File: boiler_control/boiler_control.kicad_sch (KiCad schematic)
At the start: 37 parts, among them J1 Conn_01x01, J3V3 Conn_01x03, J5V1 Conn_01x03, U2 MOUDLE-SEEEDUINO-XIAO-ESP32C3

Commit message: Replace max3856 with SSOP package; replace all 0201 res/cap packages with 0603
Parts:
- removed C1, C2, C4, C5: 100n, Capacitor_SMD:C_0201_0603Metric_Pad0.64x0.40mm_HandSolder, symbol Device:C
- removed C3, C6: 100nF, Capacitor_SMD:C_0201_0603Metric_Pad0.64x0.40mm_HandSolder, symbol Device:C
- removed JPTa1, JPTb1: Conn_01x02, Connector_PinHeader_2.54mm:PinHeader_1x02_P2.54mm_Vertical, symbol Connector_Generic:Conn_01x02
- removed R1, R2, R3, R7: 1k, Resistor_SMD:R_0201_0603Metric_Pad0.64x0.40mm_HandSolder, symbol Device:R
- removed Rref1, Rref2: R, Resistor_SMD:R_0201_0603Metric_Pad0.64x0.40mm_HandSolder, symbol Device:R
- removed UPTA1, UPTB1: MAX31865xTP, Package_DFN_QFN:TQFN-20-1EP_5x5mm_P0.65mm_EP3.25x3.25mm, symbol Sensor_Temperature:MAX31865xTP
- R4, R5, R6: footprint Resistor_SMD:R_0201_0603Metric_Pad0.64x0.40mm_HandSolder -> Resistor_SMD:R_0603_1608Metric_Pad0.98x0.95mm_HandSolder
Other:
- added sheet bottom_max (bottom_max.kicad_sch)
- note removed: "0.1%"
- note removed: "430 Ohm for PT100 4.3 kOhm for PT1000"

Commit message: Updating to v1.4 - pushed to order
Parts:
- J1: footprint Connector_PinHeader_1.00mm:PinHeader_1x01_P1.00mm_Vertical -> Connector_PinHeader_2.54mm:PinHeader_1x01_P2.54mm_Vertical
- R21: value R -> 100
- R22: value R -> 330
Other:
- moved on the sheet: D4, D5, H1, H2, H3, H4, J1, J3V3, J5V1, JDisplay1, JGND1, JGND2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

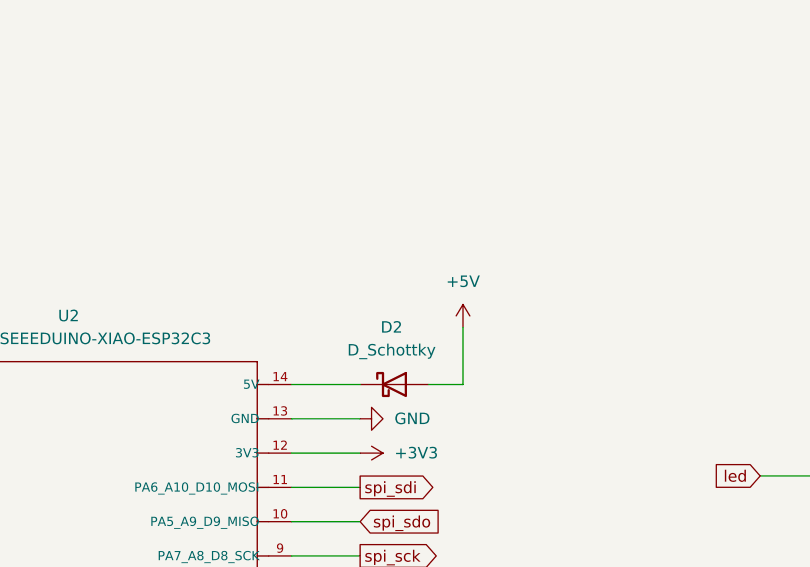
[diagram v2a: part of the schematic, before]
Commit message: Adding JB1 jumper for bridge change size of connectors for pt1000 to 3.5 mm some cosmetics
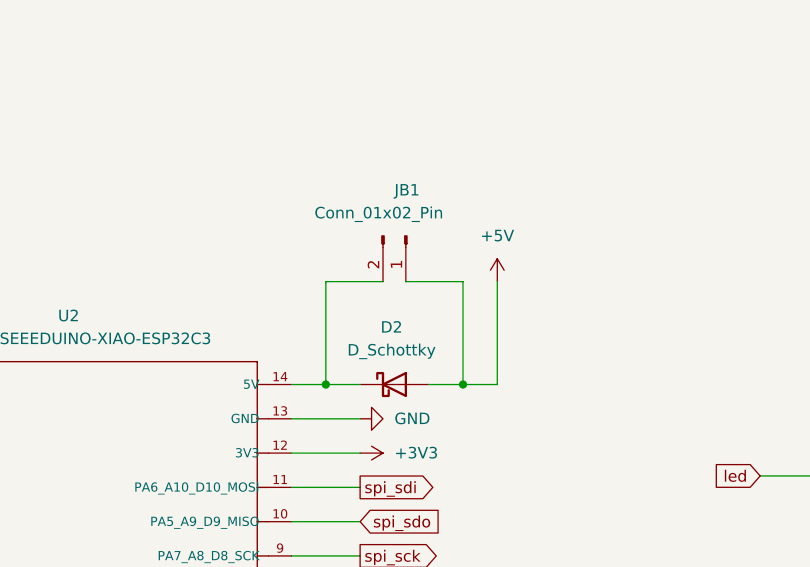
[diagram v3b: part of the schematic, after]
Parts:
- added JB1: Conn_01x02_Pin, Connector_PinHeader_2.54mm:PinHeader_1x02_P2.54mm_Vertical, symbol Connector:Conn_01x02_Pin
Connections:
- net +5V: now also JB1.1 (Pin_1)
- net at D2.1 (K), U2.14 (5V): now also JB1.2 (Pin_2)
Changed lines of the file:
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@@
   (junction (at 139.7 133.35) (diameter 0) (color 0 0 0 0)
   )
+  (junction (at 114.3 38.1) (diameter 0) (color 0 0 0 0)
+  )
   (junction (at 59.69 123.19) (diameter 0) (color 0 0 0 0)
   )
@@
   (junction (at 69.85 125.73) (diameter 0) (color 0 0 0 0)
   )
+  (junction (at 99.06 38.1) (diameter 0) (color 0 0 0 0)
+  )
   (junction (at 208.28 72.39) (diameter 0) (color 0 0 0 0)
   )
@@
     (stroke (width 0) (type default))
   )
+  (wire (pts (xy 99.06 26.67) (xy 99.06 38.1))
+    (stroke (width 0) (type default))
+  )
   (wire (pts (xy 95.25 57.15) (xy 102.87 57.15))
     (stroke (width 0) (type default))
@@
     (stroke (width 0) (type default))
   )
+  (wire (pts (xy 105.41 26.67) (xy 99.06 26.67))
+    (stroke (width 0) (type default))
+  )
   (wire (pts (xy 95.25 45.72) (xy 102.87 45.72))
     (stroke (width 0) (type default))
@@
     (stroke (width 0) (type default))
   )
+  (wire (pts (xy 118.11 26.67) (xy 118.11 38.1))
+    (stroke (width 0) (type default))
+  )
   (wire (pts (xy 95.25 53.34) (xy 102.87 53.34))
     (stroke (width 0) (type default))
@@
     (stroke (width 0) (type default))
   )
+  (wire (pts (xy 114.3 26.67) (xy 114.3 38.1))
+    (stroke (width 0) (type default))
+  )
   (wire (pts (xy 69.85 125.73) (xy 69.85 128.27))
     (stroke (width 0) (type default))
@@
     (stroke (width 0) (type default))
   )
-  (wire (pts (xy 114.3 38.1) (xy 114.3 31.75))
-    (stroke (width 0) (type default))
-  )
   (wire (pts (xy 59.69 116.84) (xy 59.69 123.19))
     (stroke (width 0) (type default))
@@
     (stroke (width 0) (type default))
   )
+  (wire (pts (xy 107.95 26.67) (xy 114.3 26.67))
+    (stroke (width 0) (type default))
+  )
   (wire (pts (xy 69.85 123.19) (xy 69.85 125.73))
     (stroke (width 0) (type default))
@@
     (stroke (width 0) (type default))
   )
+  (wire (pts (xy 114.3 38.1) (xy 118.11 38.1))
+    (stroke (width 0) (type default))
+  )
   (wire (pts (xy 66.04 139.7) (xy 69.85 139.7))
     (stroke (width 0) (type default))
   )
+  (wire (pts (xy 99.06 38.1) (xy 102.87 38.1))
+    (stroke (width 0) (type default))
+  )
   (wire (pts (xy 38.1 60.96) (xy 45.72 60.96))
     (stroke (width 0) (type default))
@@
     (stroke (width 0) (type default))
   )
-  (wire (pts (xy 95.25 38.1) (xy 102.87 38.1))
+  (wire (pts (xy 95.25 38.1) (xy 99.06 38.1))
     (stroke (width 0) (type default))
   )
@@
     )
   )
+  (symbol (lib_id "Connector:Conn_01x02_Pin") (at 107.95 21.59 270) (unit 1)
+    (in_bom yes) (on_board yes) (dnp no)
+    (property "Reference" "JB1" (at 106.68 16.51 90)
+      (effects (font (size 1.27 1.27)) (justify left))
+    )
+    (property "Value" "Conn_01x02_Pin" (at 97.79 19.05 90)
+      (effects (font (size 1.27 1.27)) (justify left))
+    )
+    (property "Footprint" "Connector_PinHeader_2.54mm:PinHeader_1x02_P2.54mm_Vertical" (at 107.95 21.59 0)
+      (effects (font (size 1.27 1.27)) hide)
+    )
+    (property "Datasheet" "~" (at 107.95 21.59 0)
+      (effects (font (size 1.27 1.27)) hide)
+    )
+    (pin "1")
+    (pin "2")
+    (instances
+      (project "boiler_control"
+        (path "/42805374-cffb-434a-be29-e600a36be254"
+          (reference "JB1") (unit 1)
+        )
+      )
+    )
+  )
   (symbol (lib_id "Device:R") (at 208.28 64.77 0) (unit 1)
     (in_bom yes) (on_board yes) (dnp no) (fields_autoplaced)
@@
     )
   )
-  (symbol (lib_id "power:+5V") (at 114.3 31.75 0) (unit 1)
-    (in_bom yes) (on_board yes) (dnp no) (fields_autoplaced)
-    (property "Reference" "#PWR02" (at 114.3 35.56 0)
-      (effects (font (size 1.27 1.27)) hide)
-    )
-    (property "Value" "+5V" (at 114.3 26.67 0)
+  (symbol (lib_id "power:+5V") (at 118.11 26.67 0) (unit 1)
+    (in_bom yes) (on_board yes) (dnp no) (fields_autoplaced)
+    (property "Reference" "#PWR02" (at 118.11 30.48 0)
+      (effects (font (size 1.27 1.27)) hide)
+    )
+    (property "Value" "+5V" (at 118.11 21.59 0)
       (effects (font (size 1.27 1.27)))
     )
-    (property "Footprint" "" (at 114.3 31.75 0)
-      (effects (font (size 1.27 1.27)) hide)
-    )
-    (property "Datasheet" "" (at 114.3 31.75 0)
-      (effects (font (size 1.27 1.27)) hide)
-    )
+    (property "Footprint" "" (at 118.11 26.67 0)
+      (effects (font (size 1.27 1.27)) hide)
+    )
+    (property "Datasheet" "" (at 118.11 26.67 0)
+      (effects (font (size 1.27 1.27)) hide)
+    )
